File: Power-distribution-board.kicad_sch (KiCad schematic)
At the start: 79 parts, among them J1 MRCBP-V-40A, J10 2606-1104/020-000, J12 2606-1104/020-000, J13 2606-1104/020-000, J15 2606-1104/020-000, J16 2606-1104/020-000, J2 MRCBP-V-40A, J3 MRCBP-V-40A, J4 MRCBP-V-40A, J5 MRCBP-V-40A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

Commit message: Finalize schematics
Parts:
- C2: value 0.1 uF -> 0.1u
- C7: value .47uF -> .47u
- C8: value 33uF -> 33u
- R1: value 240 ohm -> 240
- R2: value 715 ohm -> 715
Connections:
- net 5VOUT is gone; now on net 5V: C10.2, C13.2, C32.1, C7.1, D4.1 (K), R1.1, U11.3 (VCC), U2.1 (IN), U4.2 (VO)
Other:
- note removed: "Note: Unfinished TO DO: BATTERY VOLTAGE MONITOR CONNECTIONS TO AUXILIARY BATTERY ESP CIRCUIT"
- note removed: "from BATTERY"
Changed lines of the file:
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@@
 		)
 	)
-	(text "from BATTERY"
-		(exclude_from_sim no)
-		(at 281.432 166.37 0)
-		(effects
-			(font
-				(size 1.27 1.27)
-			)
-		)
-	)
 	(text "I2C Address: 0x41"
 		(exclude_from_sim no)
@@
 		)
 	)
-	(text "Note: Unfinished\n\nTO DO:\nBATTERY VOLTAGE MONITOR\nCONNECTIONS TO AUXILIARY BATTERY\nESP CIRCUIT\n\n"
-		(exclude_from_sim no)
-		(at 16.51 22.86 0)
-		(effects
-			(font
-				(size 1.27 1.27)
-			)
-			(justify left)
-		)
-	)
 	(text "USB Stackup\n"
 		(exclude_from_sim no)
@@
 		)
 	)
-	(label "5VOUT"
+	(label "5V"
 		(at 430.53 167.64 0)
 		(effects
@@
 		)
 	)
-	(label "5VOUT"
+	(label "5V"
 		(at 445.77 36.83 0)
 		(effects
@@
 		)
 	)
-	(label "5VOUT"
+	(label "IC4"
+		(at 156.21 104.14 0)
+		(effects
+			(font
+				(size 1.27 1.27)
+			)
+			(justify left bottom)
+		)
+	)
+	(label "IC6"
+		(at 156.21 124.46 0)
+		(effects
+			(font
+				(size 1.27 1.27)
+			)
+			(justify left bottom)
+		)
+	)
+	(label "5V"
 		(at 311.15 87.63 180)
 		(effects
@@
 		)
 	)
-	(label "5VOUT"
+	(label "5V"
 		(at 360.68 274.32 180)
 		(effects
@@
 			)
 		)
-		(property "Value" ".47uF"
+		(property "Value" ".47u"
 			(at 369.57 288.2899 0)
 			(effects
@@
 			)
 		)
-		(property "Value" "33uF"
+		(property "Value" "33u"
 			(at 422.91 289.5599 0)
 			(effects
@@
 			)
 		)
-		(property "Value" "715 ohm"
+		(property "Value" "715"
 			(at 364.49 191.7699 0)
 			(effects
@@
 			)
 		)
-		(property "Value" "240 ohm"
+		(property "Value" "240"
 			(at 389.89 176.5299 0)
 			(effects
@@
 			)
 		)
-		(property "Value" "0.1 uF"
+		(property "Value" "0.1u"
 			(at 344.17 179.0699 0)
 			(effects

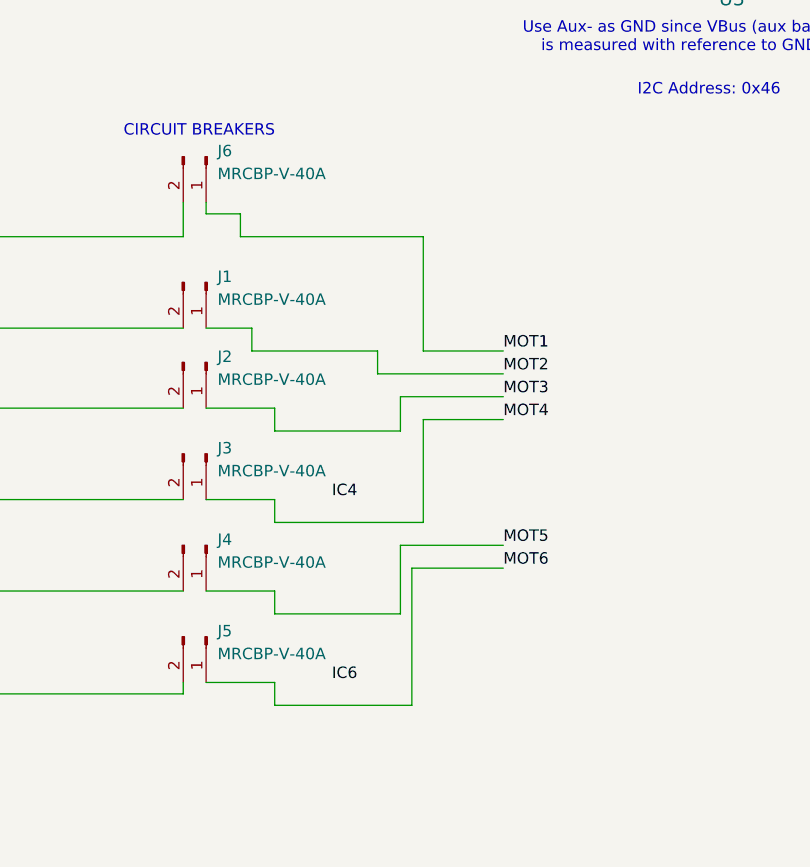
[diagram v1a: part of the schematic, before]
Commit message: Changed breaker labels and added all footprints
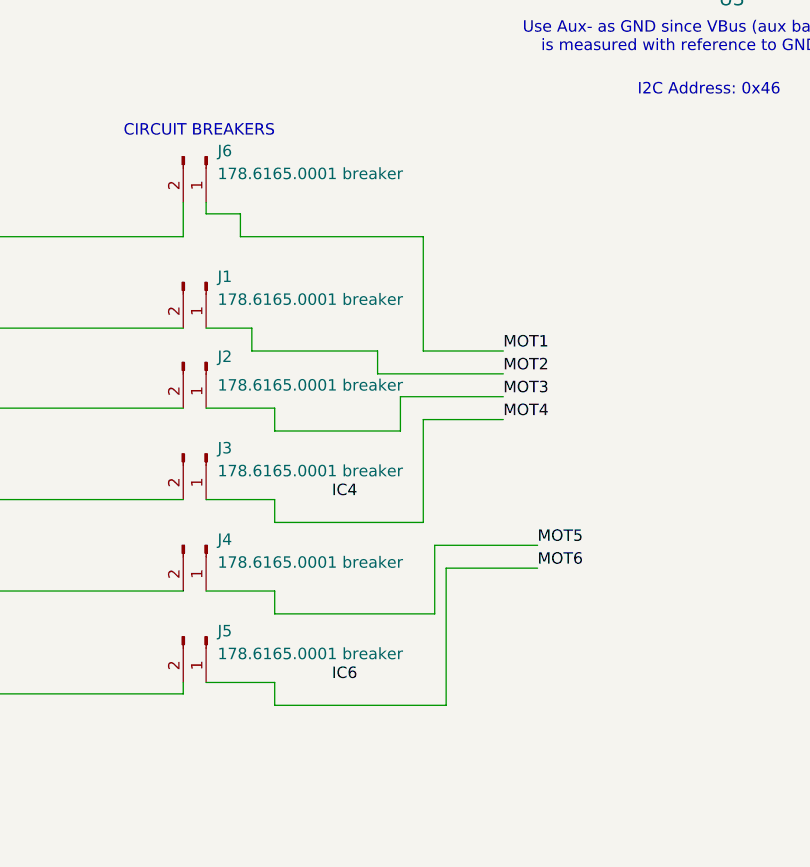
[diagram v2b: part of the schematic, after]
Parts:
- C1, C11, C12, C14, C15, C16, C17, C18, C19, C2, C20, C21, C22, C23, C32, C7, C8: footprint (none) -> Capacitor_SMD:C_0805_2012Metric
- J1, J2, J3, J4, J5, J6: value MRCBP-V-40A -> 178.6165.0001 breaker; footprint (none) -> Custom:CONN_178.6165.0001_LTF
- R1, R10, R12, R13, R14, R2, R22, R23, R24, R25, R26, R27, R28, R29, R30, R31, R32, R33, R8, R9: footprint (none) -> Resistor_SMD:R_0805_2012Metric
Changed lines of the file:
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@@
 	(wire
 		(pts
-			(xy 165.1 127) (xy 165.1 111.76)
+			(xy 168.91 127) (xy 168.91 111.76)
 		)
 		(stroke
@@
 	(wire
 		(pts
-			(xy 149.86 116.84) (xy 163.83 116.84)
+			(xy 149.86 116.84) (xy 167.64 116.84)
 		)
 		(stroke
@@
 	(wire
 		(pts
-			(xy 163.83 116.84) (xy 163.83 109.22)
+			(xy 167.64 116.84) (xy 167.64 109.22)
 		)
 		(stroke
@@
 	(wire
 		(pts
-			(xy 165.1 111.76) (xy 175.26 111.76)
+			(xy 168.91 111.76) (xy 179.07 111.76)
 		)
 		(stroke
@@
 	(wire
 		(pts
-			(xy 163.83 109.22) (xy 175.26 109.22)
+			(xy 167.64 109.22) (xy 179.07 109.22)
 		)
 		(stroke
@@
 	(wire
 		(pts
-			(xy 149.86 127) (xy 165.1 127)
+			(xy 149.86 127) (xy 168.91 127)
 		)
 		(stroke
@@
 	)
 	(label "MOT6"
-		(at 175.26 111.76 0)
+		(at 179.07 111.76 0)
 		(effects
 			(font
@@
 	)
 	(label "MOT5"
-		(at 175.26 109.22 0)
+		(at 179.07 109.22 0)
 		(effects
 			(font
@@
 			)
 		)
-		(property "Footprint" ""
+		(property "Footprint" "Capacitor_SMD:C_0805_2012Metric"
 			(at 92.4052 289.56 0)
 			(effects
@@
 			)
 		)
-		(property "Footprint" ""
+		(property "Footprint" "Resistor_SMD:R_0805_2012Metric"
 			(at 204.47 225.552 90)
 			(effects
@@
 			)
 		)
-		(property "Value" "MRCBP-V-40A"
+		(property "Value" "178.6165.0001 breaker"
 			(at 143.51 121.2849 90)
 			(effects
@@
 			)
 		)
-		(property "Footprint" ""
+		(property "Footprint" "Custom:CONN_178.6165.0001_LTF"
 			(at 142.24 119.38 0)
 			(effects
@@
 			)
 		)
-		(property "Footprint" ""
+		(property "Footprint" "Resistor_SMD:R_0805_2012Metric"
 			(at 105.41 264.668 90)
 			(effects
@@
 			)
 		)
-		(property "Footprint" ""
+		(property "Footprint" "Capacitor_SMD:C_0805_2012Metric"
 			(at 94.9452 245.11 0)
 			(effects
@@
 			)
 		)
-		(property "Footprint" ""
+		(property "Footprint" "Capacitor_SMD:C_0805_2012Metric"
 			(at 199.0852 226.06 0)
 			(effects
@@
 			)
 		)
-		(property "Footprint" ""
+		(property "Footprint" "Capacitor_SMD:C_0805_2012Metric"
 			(at 366.7252 290.83 0)
 			(effects
@@
 			)
 		)
-		(property "Footprint" ""
+		(property "Footprint" "Resistor_SMD:R_0805_2012Metric"
 			(at 203.2 272.542 90)
 			(effects
@@
 			)
 		)
-		(property "Value" "MRCBP-V-40A"
+		(property "Value" "178.6165.0001 breaker"
 			(at 143.51 81.9149 90)
 			(effects
@@
 			)
 		)
-		(property "Footprint" ""
+		(property "Footprint" "Custom:CONN_178.6165.0001_LTF"
 			(at 142.24 80.01 0)
 			(effects
@@
 			)
 		)
-		(property "Footprint" ""
+		(property "Footprint" "Capacitor_SMD:C_0805_2012Metric"
 			(at 190.1952 289.56 0)
 			(effects
@@
 			)
 		)
-		(property "Footprint" ""
+		(property "Footprint" "Capacitor_SMD:C_0805_2012Metric"
 			(at 102.5652 228.6 0)
 			(effects
@@
 			)
 		)
-		(property "Footprint" ""
+		(property "Footprint" "Resistor_SMD:R_0805_2012Metric"
 			(at 117.348 313.69 90)
 			(effects
@@
 			)
 		)
-		(property "Footprint" ""
+		(property "Footprint" "Resistor_SMD:R_0805_2012Metric"
 			(at 216.408 219.71 90)
 			(effects
@@
 			)
 		)
-		(property "Footprint" ""
+		(property "Footprint" "Capacitor_SMD:C_0805_2012Metric"
 			(at 190.1952 335.28 0)
 			(effects
@@
 			)
 		)
-		(property "Footprint" ""
+		(property "Footprint" "Capacitor_SMD:C_0805_2012Metric"
 			(at 191.4652 242.57 0)
 			(effects
@@
 			)
 		)
-		(property "Footprint" ""
+		(property "Footprint" "Resistor_SMD:R_0805_2012Metric"
 			(at 204.47 217.678 90)
 			(effects
@@
 			)
 		)
-		(property "Value" "MRCBP-V-40A"
+		(property "Value" "178.6165.0001 breaker"
 			(at 143.51 100.9649 90)
 			(effects
@@
 			)
 		)
-		(property "Footprint" ""
+		(property "Footprint" "Custom:CONN_178.6165.0001_LTF"
 			(at 142.24 99.06 0)
 			(effects
@@
 		(on_board yes)
 		(dnp no)
-		(fields_autoplaced yes)
 		(property "Reference" "J2"
 			(at 143.51 88.2649 90)
@@
 			)
 		)
-		(property "Value" "MRCBP-V-40A"
-			(at 143.51 90.8049 90)
+		(property "Value" "178.6165.0001 breaker"
+			(at 143.51 91.44 90)
 			(effects
 				(font
@@
 			)
 		)
-		(property "Footprint" ""
+		(property "Footprint" "Custom:CONN_178.6165.0001_LTF"
 			(at 142.24 88.9 0)
 			(effects
@@
 			)
 		)
-		(property "Footprint" ""
+		(property "Footprint" "Resistor_SMD:R_0805_2012Metric"
 			(at 105.41 272.542 90)
 			(effects
@@
 			)
 		)
-		(property "Footprint" ""
+		(property "Footprint" "Capacitor_SMD:C_0805_2012Metric"
 			(at 197.8152 318.77 0)
 			(effects
@@
 			)
 		)
-		(property "Value" "MRCBP-V-40A"
+		(property "Value" "178.6165.0001 breaker"
 			(at 143.51 111.1249 90)
 			(effects
@@
 			)
 		)
-		(property "Footprint" ""
+		(property "Footprint" "Custom:CONN_178.6165.0001_LTF"
 			(at 142.24 109.22 0)
 			(effects
@@
 			)
 		)
-		(property "Value" "MRCBP-V-40A"
+		(property "Value" "178.6165.0001 breaker"
 			(at 143.51 67.9449 90)
 			(effects
@@
 			)
 		)
-		(property "Footprint" ""
+		(property "Footprint" "Custom:CONN_178.6165.0001_LTF"
 			(at 142.24 66.04 0)
 			(effects
@@
 			)
 		)
-		(property "Footprint" ""
+		(property "Footprint" "Capacitor_SMD:C_0805_2012Metric"
 			(at 92.4052 336.55 0)
 			(effects
@@
 			)
 		)
-		(property "Footprint" ""
+		(property "Footprint" "Capacitor_SMD:C_0805_2012Metric"
 			(at 420.0652 292.1 0)
 			(effects
@@
 			)
 		)
-		(property "Footprint" ""
+		(property "Footprint" "Resistor_SMD:R_0805_2012Metric"
 			(at 215.138 312.42 90)
 			(effects
@@
 			)
 		)
-		(property "Footprint" ""
+		(property "Footprint" "Resistor_SMD:R_0805_2012Metric"
 			(at 360.172 190.5 90)
 			(effects
@@
 			)
 		)
-		(property "Footprint" ""
+		(property "Footprint" "Resistor_SMD:R_0805_2012Metric"
 			(at 107.95 228.092 90)
 			(effects
@@
 			)
 		)
-		(property "Footprint" ""
+		(property "Footprint" "Resistor_SMD:R_0805_2012Metric"
 			(at 117.348 266.7 90)
 			(effects
@@
 			)
 		)
-		(property "Footprint" ""
+		(property "Footprint" "Capacitor_SMD:C_0805_2012Metric"
 			(at 100.0252 320.04 0)
 			(effects
@@
 			)
 		)
-		(property "Footprint" ""
+		(property "Footprint" "Resistor_SMD:R_0805_2012Metric"
 			(at 107.95 220.218 90)
 			(effects
@@
 			)
 		)
-		(property "Footprint" ""
+		(property "Footprint" "Capacitor_SMD:C_0805_2012Metric"
 			(at 417.5252 181.61 0)
 			(effects
@@
 			)
 		)
-		(property "Footprint" ""
+		(property "Footprint" "Resistor_SMD:R_0805_2012Metric"
 			(at 105.41 319.532 90)
 			(effects
@@
 			)
 		)
-		(property "Footprint" ""
+		(property "Footprint" "Resistor_SMD:R_0805_2012Metric"
 			(at 215.138 266.7 90)
 			(effects
@@
 			)
 		)
-		(property "Footprint" ""
+		(property "Footprint" "Capacitor_SMD:C_0805_2012Metric"
 			(at 197.8152 273.05 0)
 			(effects
@@
 			)
 		)
-		(property "Footprint" ""
+		(property "Footprint" "Resistor_SMD:R_0805_2012Metric"
 			(at 203.2 264.668 90)
 			(effects
@@
 			)
 		)
-		(property "Footprint" ""
+		(property "Footprint" "Resistor_SMD:R_0805_2012Metric"
 			(at 203.2 310.388 90)
 			(effects
@@
 			)
 		)
-		(property "Footprint" ""
+		(property "Footprint" "Resistor_SMD:R_0805_2012Metric"
 			(at 203.2 318.262 90)
 			(effects
@@
 			)
 		)
-		(property "Footprint" ""
+		(property "Footprint" "Resistor_SMD:R_0805_2012Metric"
 			(at 385.572 175.26 90)
 			(effects
@@
 			)
 		)
-		(property "Footprint" ""
+		(property "Footprint" "Capacitor_SMD:C_0805_2012Metric"
 			(at 181.9148 22.86 0)
 			(effects
@@
 			)
 		)
-		(property "Footprint" ""
+		(property "Footprint" "Resistor_SMD:R_0805_2012Metric"
 			(at 105.41 311.658 90)
 			(effects
@@
 			)
 		)
-		(property "Footprint" ""
+		(property "Footprint" "Capacitor_SMD:C_0805_2012Metric"
 			(at 100.0252 273.05 0)
 			(effects
@@
 			)
 		)
-		(property "Footprint" ""
+		(property "Footprint" "Resistor_SMD:R_0805_2012Metric"
 			(at 119.888 223.52 90)
 			(effects
@@
 			)
 		)
-		(property "Footprint" ""
+		(property "Footprint" "Capacitor_SMD:C_0805_2012Metric"
 			(at 341.3252 181.61 0)
 			(effects

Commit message: fixed footprints error, begun pcb design
added footprints into project and started pcb design
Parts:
- D4: footprint Diode_SMD:USC-TOS -> pdb_footprints:USC_TOS
- J1, J2, J3, J4, J5, J6: footprint Custom:CONN_178.6165.0001_LTF -> pdb_footprints:CONN_178.6165.0001_LTF
- J10, J12, J13, J15, J16: footprint CONN4_2606-1104/020-000_WAG -> pdb_footprints:CONN4_2606-1104&slash_020-000_WAG
- U12, U13, U14, U15, U16, U17, U3: footprint DGS10 -> pdb_footprints:DGS10
- U2: footprint LM3940IT-3.3:TO254P1054X470X1955-3 -> pdb_footprints:T03B
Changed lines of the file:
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@@
 			)
 		)
-		(property "Footprint" "Diode_SMD:USC-TOS"
+		(property "Footprint" "pdb_footprints:USC_TOS"
 			(at 445.77 45.72 0)
 			(effects
@@
 			)
 		)
-		(property "Footprint" "DGS10"
+		(property "Footprint" "pdb_footprints:DGS10"
 			(at 157.48 271.78 0)
 			(effects
@@
 			)
 		)
-		(property "Footprint" "Custom:CONN_178.6165.0001_LTF"
+		(property "Footprint" "pdb_footprints:CONN_178.6165.0001_LTF"
 			(at 142.24 119.38 0)
 			(effects
@@
 			)
 		)
-		(property "Footprint" "CONN4_2606-1104/020-000_WAG"
+		(property "Footprint" "pdb_footprints:CONN4_2606-1104&slash_020-000_WAG"
 			(at 142.24 148.59 0)
 			(effects
@@
 			)
 		)
-		(property "Footprint" "Custom:CONN_178.6165.0001_LTF"
+		(property "Footprint" "pdb_footprints:CONN_178.6165.0001_LTF"
 			(at 142.24 80.01 0)
 			(effects
@@
 			)
 		)
-		(property "Footprint" "CONN4_2606-1104/020-000_WAG"
+		(property "Footprint" "pdb_footprints:CONN4_2606-1104&slash_020-000_WAG"
 			(at 90.17 71.12 0)
 			(effects
@@
 			)
 		)
-		(property "Footprint" "LM3940IT-3.3:TO254P1054X470X1955-3"
+		(property "Footprint" "pdb_footprints:T03B"
 			(at 392.43 276.86 0)
 			(effects
@@
 			)
 		)
-		(property "Footprint" "Custom:CONN_178.6165.0001_LTF"
+		(property "Footprint" "pdb_footprints:CONN_178.6165.0001_LTF"
 			(at 142.24 99.06 0)
 			(effects
@@
 			)
 		)
-		(property "Footprint" "Custom:CONN_178.6165.0001_LTF"
+		(property "Footprint" "pdb_footprints:CONN_178.6165.0001_LTF"
 			(at 142.24 88.9 0)
 			(effects
@@
 			)
 		)
-		(property "Footprint" "Custom:CONN_178.6165.0001_LTF"
+		(property "Footprint" "pdb_footprints:CONN_178.6165.0001_LTF"
 			(at 142.24 109.22 0)
 			(effects
@@
 			)
 		)
-		(property "Footprint" "Custom:CONN_178.6165.0001_LTF"
+		(property "Footprint" "pdb_footprints:CONN_178.6165.0001_LTF"
 			(at 142.24 66.04 0)
 			(effects
@@
 			)
 		)
-		(property "Footprint" "DGS10"
+		(property "Footprint" "pdb_footprints:DGS10"
 			(at 59.69 271.78 0)
 			(effects
@@
 			)
 		)
-		(property "Footprint" "CONN4_2606-1104/020-000_WAG"
+		(property "Footprint" "pdb_footprints:CONN4_2606-1104&slash_020-000_WAG"
 			(at 142.24 181.61 0)
 			(effects
@@
 			)
 		)
-		(property "Footprint" "DGS10"
+		(property "Footprint" "pdb_footprints:DGS10"
 			(at 59.69 318.77 0)
 			(effects
@@
 			)
 		)
-		(property "Footprint" "DGS10"
+		(property "Footprint" "pdb_footprints:DGS10"
 			(at 158.75 224.79 0)
 			(effects
@@
 			)
 		)
-		(property "Footprint" "DGS10"
+		(property "Footprint" "pdb_footprints:DGS10"
 			(at 62.23 227.33 0)
 			(effects
@@
 			)
 		)
-		(property "Footprint" "DGS10"
+		(property "Footprint" "pdb_footprints:DGS10"
 			(at 214.63 40.64 0)
 			(effects
@@
 			)
 		)
-		(property "Footprint" "DGS10"
+		(property "Footprint" "pdb_footprints:DGS10"
 			(at 157.48 317.5 0)
 			(effects
@@
 			)
 		)
-		(property "Footprint" "CONN4_2606-1104/020-000_WAG"
+		(property "Footprint" "pdb_footprints:CONN4_2606-1104&slash_020-000_WAG"
 			(at 200.66 149.86 0)
 			(effects
@@
 			)
 		)
-		(property "Footprint" "CONN4_2606-1104/020-000_WAG"
+		(property "Footprint" "pdb_footprints:CONN4_2606-1104&slash_020-000_WAG"
 			(at 142.24 166.37 0)
 			(effects

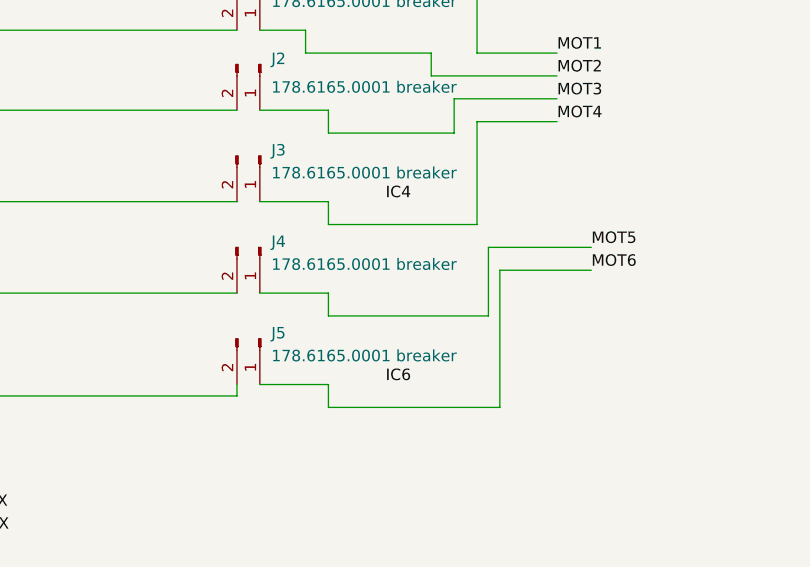
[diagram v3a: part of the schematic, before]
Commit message: work on pcb editor
changed layout of components, changed to 4 layer pcb, set minimum trace width 0.2mm
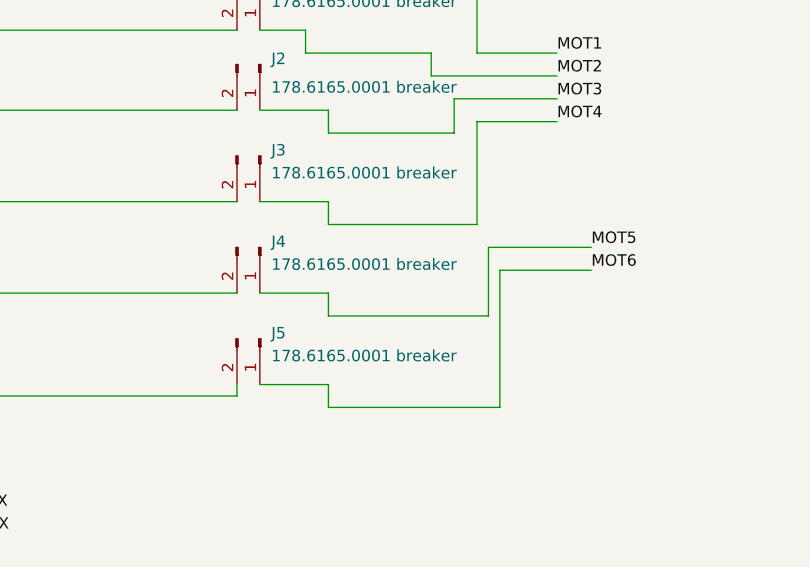
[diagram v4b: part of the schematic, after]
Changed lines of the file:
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@@
-		)
-	)
-	(label "IC4"
-		(at 156.21 104.14 0)
-		(effects
-			(font
-				(size 1.27 1.27)
-			)
-			(justify left bottom)
-		)
-	)
-	(label "IC6"
-		(at 156.21 124.46 0)
-		(effects
-			(font
-				(size 1.27 1.27)
-			)
-			(justify left bottom)
 		)
 	)

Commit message: set layout
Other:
- moved on the sheet: C12, C14, C15, C17, R12, R13, R14, R22, R23, R24, U13, U14
